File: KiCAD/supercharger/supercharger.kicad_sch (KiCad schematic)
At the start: 25 parts, among them J2 BAT, J4 UJC-H-G-SMT-1-P6-TR

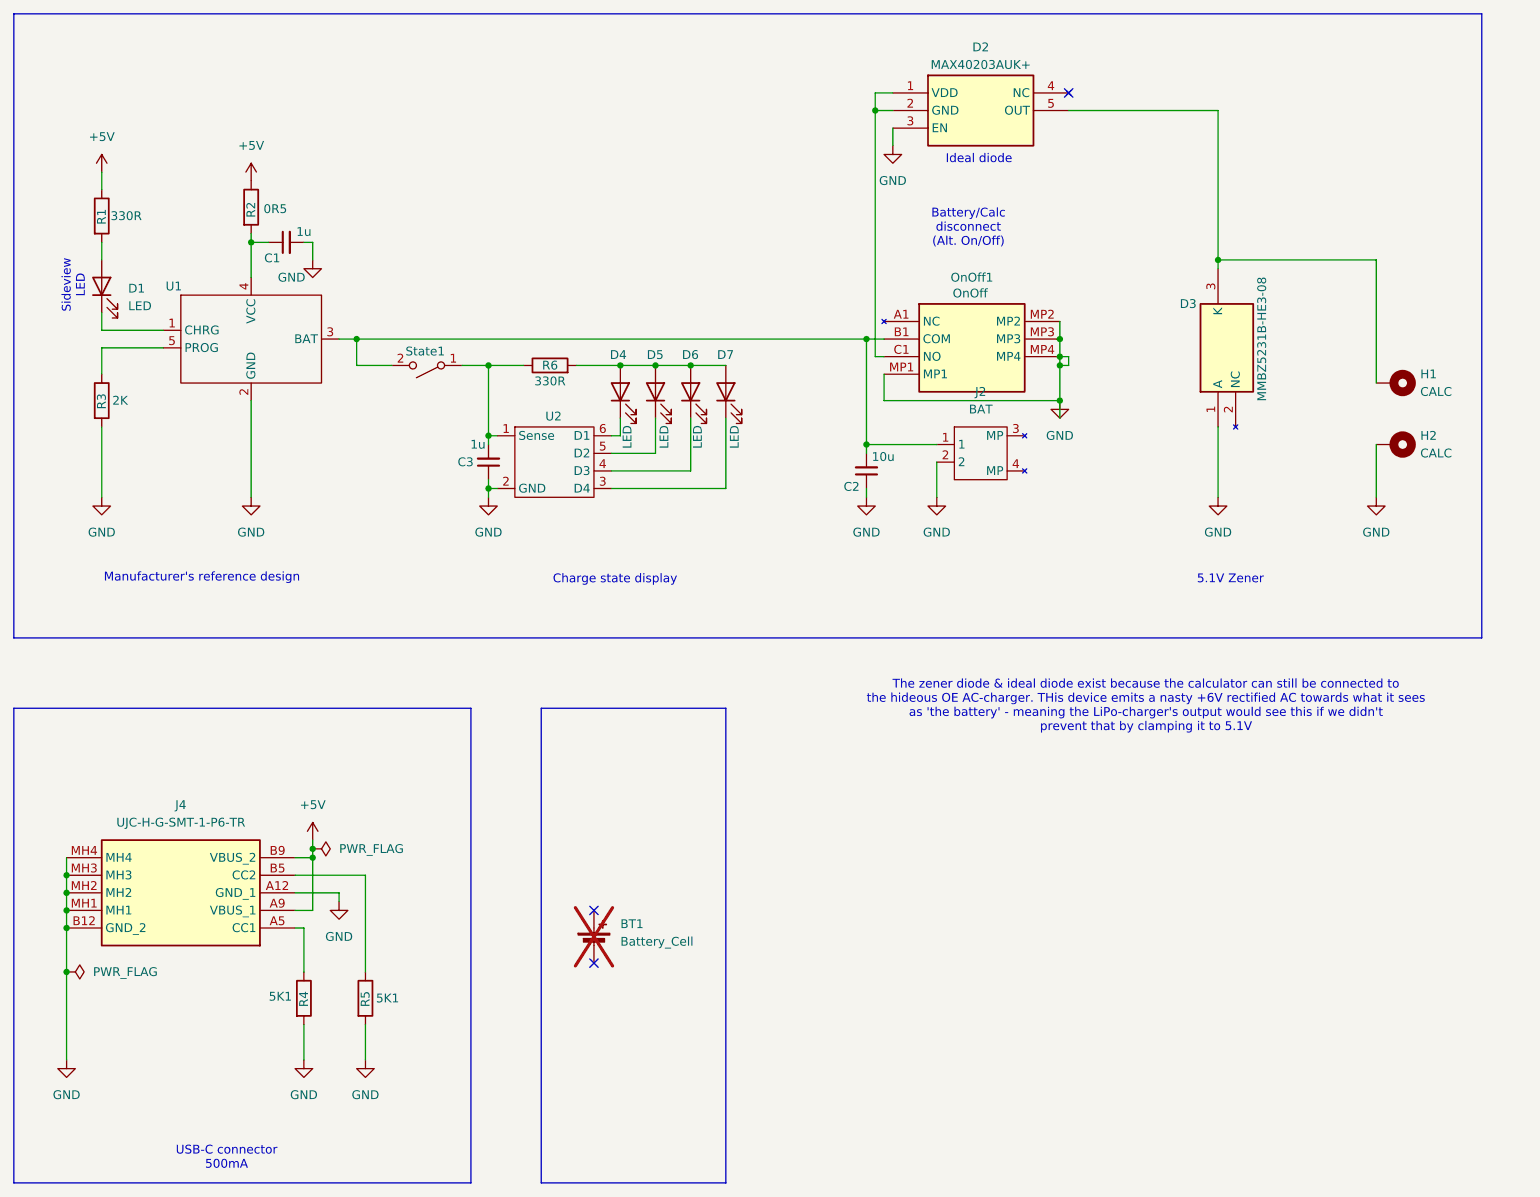
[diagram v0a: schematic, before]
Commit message: Schematic documentation update
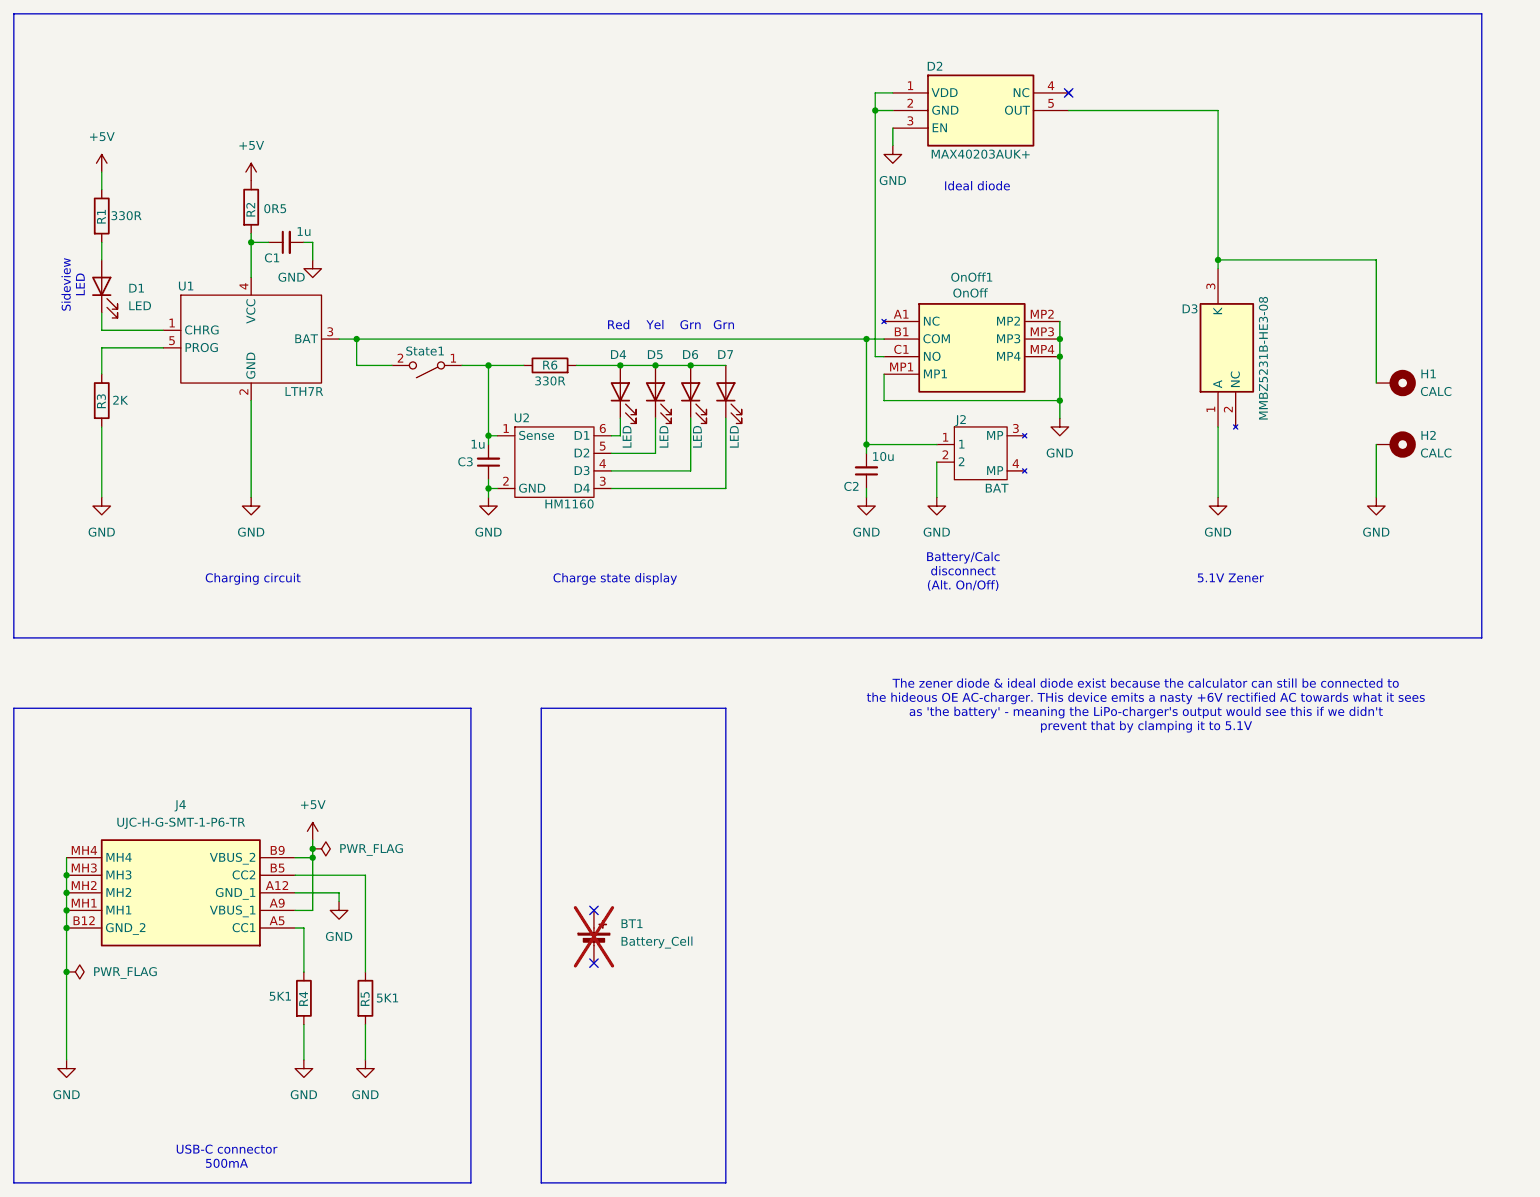
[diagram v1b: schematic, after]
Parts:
- U1: value ~ -> LTH7R
- U2: value ~ -> HM1160
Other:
- note added: "Charging circuit"
- note added: "Grn"
- note added: "Red"
- note added: "Yel"
- note removed: "Manufacturer's reference design"
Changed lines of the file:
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@@
 	)
 	(junction
-		(at 171.45 71.12)
-		(diameter 0)
-		(color 0 0 0 0)
-	)
-	(junction
 		(at 63.5 140.97)
 		(diameter 0)
@@
 	(wire
 		(pts
-			(xy 171.45 69.85) (xy 171.45 71.12)
+			(xy 171.45 69.85) (xy 171.45 76.2)
 		)
 		(stroke
@@
 	(wire
 		(pts
-			(xy 172.72 71.12) (xy 172.72 69.85)
-		)
-		(stroke
-			(width 0)
-			(type default)
-		)
-	)
-	(wire
-		(pts
 			(xy 67.31 147.32) (xy 60.96 147.32)
 		)
@@
 	(wire
 		(pts
-			(xy 171.45 71.12) (xy 171.45 76.2)
-		)
-		(stroke
-			(width 0)
-			(type default)
-		)
-	)
-	(wire
-		(pts
 			(xy 71.12 144.78) (xy 71.12 158.75)
 		)
@@
 	(wire
 		(pts
-			(xy 172.72 69.85) (xy 171.45 69.85)
-		)
-		(stroke
-			(width 0)
-			(type default)
-		)
-	)
-	(wire
-		(pts
 			(xy 146.05 76.2) (xy 171.45 76.2)
 		)
@@
 	(wire
 		(pts
-			(xy 171.45 78.74) (xy 171.45 76.2)
-		)
-		(stroke
-			(width 0)
-			(type default)
-		)
-	)
-	(wire
-		(pts
 			(xy 88.9 88.9) (xy 88.9 90.17)
 		)
@@
 	(wire
 		(pts
+			(xy 171.45 78.74) (xy 171.45 76.2)
+		)
+		(stroke
+			(width 0)
+			(type default)
+		)
+	)
+	(wire
+		(pts
 			(xy 153.67 85.09) (xy 153.67 90.17)
 		)
@@
 	(wire
 		(pts
-			(xy 172.72 71.12) (xy 171.45 71.12)
-		)
-		(stroke
-			(width 0)
-			(type default)
-		)
-	)
-	(wire
-		(pts
 			(xy 146.05 72.39) (xy 146.05 76.2)
 		)
@@
 		)
 	)
+	(text "Red"
+		(exclude_from_sim no)
+		(at 107.696 65.532 0)
+		(effects
+			(font
+				(size 1.27 1.27)
+			)
+		)
+	)
+	(text "Grn"
+		(exclude_from_sim no)
+		(at 118.11 65.532 0)
+		(effects
+			(font
+				(size 1.27 1.27)
+			)
+		)
+	)
 	(text "Sideview\nLED"
 		(exclude_from_sim no)
@@
 		)
 	)
+	(text "Grn"
+		(exclude_from_sim no)
+		(at 122.936 65.532 0)
+		(effects
+			(font
+				(size 1.27 1.27)
+			)
+		)
+	)
+	(text "Yel"
+		(exclude_from_sim no)
+		(at 113.03 65.532 0)
+		(effects
+			(font
+				(size 1.27 1.27)
+			)
+		)
+	)
 	(text "Battery/Calc\ndisconnect\n(Alt. On/Off)"
 		(exclude_from_sim no)
-		(at 158.242 51.308 0)
+		(at 157.48 101.092 0)
 		(effects
 			(font
@@
 	(text "Ideal diode"
 		(exclude_from_sim no)
-		(at 159.766 41.402 0)
+		(at 159.512 45.466 0)
 		(effects
 			(font
@@
 		)
 	)
-	(text "Manufacturer's reference design"
+	(text "Charging circuit"
 		(exclude_from_sim yes)
-		(at 47.498 101.854 0)
+		(at 54.864 102.108 0)
 		(effects
 			(font
@@
 		(dnp no)
 		(property "Reference" "D2"
-			(at 160.02 25.146 0)
+			(at 153.416 27.94 0)
 			(effects
 				(font
@@
 		)
 		(property "Value" "MAX40203AUK+"
-			(at 160.02 27.686 0)
+			(at 160.02 40.64 0)
 			(effects
 				(font
@@
 			)
 		)
-		(property "Datasheet" "~"
+		(property "Datasheet" "https://www.digikey.com/en/products/detail/omron-electronics-inc-emc-div/B3U-3000PM-B/2754806"
 			(at 80.01 71.12 0)
 			(effects
@@
 	(symbol
 		(lib_id "power:GND")
-		(at 171.45 76.2 0)
+		(at 171.45 78.74 0)
 		(unit 1)
 		(exclude_from_sim no)
@@
 		(fields_autoplaced yes)
 		(property "Reference" "#PWR014"
-			(at 171.45 82.55 0)
+			(at 171.45 85.09 0)
 			(effects
 				(font
@@
 		)
 		(property "Value" "GND"
-			(at 171.45 81.28 0)
+			(at 171.45 83.82 0)
 			(effects
 				(font
@@
 		)
 		(property "Footprint" ""
-			(at 171.45 76.2 0)
+			(at 171.45 78.74 0)
 			(effects
 				(font
@@
 		)
 		(property "Datasheet" ""
-			(at 171.45 76.2 0)
+			(at 171.45 78.74 0)
 			(effects
 				(font
@@
 		)
 		(property "Description" "Power symbol creates a global label with name \"GND\" , ground"
-			(at 171.45 76.2 0)
+			(at 171.45 78.74 0)
 			(effects
 				(font
@@
 		(on_board yes)
 		(dnp no)
-		(fields_autoplaced yes)
 		(property "Reference" "J2"
-			(at 160.02 74.93 0)
+			(at 157.226 78.994 0)
 			(effects
 				(font
@@
 		)
 		(property "Value" "BAT"
-			(at 160.02 77.47 0)
+			(at 162.306 88.9 0)
 			(effects
 				(font
@@
 		(dnp no)
 		(property "Reference" "D3"
-			(at 189.992 62.23 90)
+			(at 190.246 62.992 90)
 			(effects
 				(font
@@
 		)
 		(property "Value" "MMBZ5231B-HE3-08"
-			(at 200.66 67.31 0)
+			(at 200.914 70.104 0)
 			(effects
 				(font
@@
 			)
 		)
-		(property "Datasheet" "https://www.arrow.com/en/products/mmbz5231b-he3-08/vishay"
+		(property "Datasheet" "https://www.digikey.dk/da/products/detail/vishay-general-semiconductor-diodes-division/MMBZ5231B-HE3-08/4832016"
 			(at 389.23 60.96 0)
 			(effects
@@
 		(dnp no)
 		(property "Reference" "U1"
-			(at 43.434 59.69 0)
+			(at 45.212 59.69 0)
 			(effects
 				(font
@@
 			)
 		)
-		(property "Value" "~"
-			(at 67.31 64.1665 0)
+		(property "Value" "LTH7R"
+			(at 62.23 74.93 0)
 			(effects
 				(font
@@
 		(dnp no)
 		(property "Reference" "U2"
-			(at 98.298 78.486 0)
+			(at 93.726 78.74 0)
 			(effects
 				(font
@@
 			)
 		)
-		(property "Value" "~"
-			(at 98.425 78.74 0)
+		(property "Value" "HM1160"
+			(at 100.584 91.186 0)
 			(effects
 				(font
@@
 			)
 		)
-		(property "Datasheet" ""
+		(property "Datasheet" "https://www.alldatasheet.com/datasheet-pdf/view/1297703/HMSEMI/HM1160.html"
 			(at 96.52 78.74 0)
 			(effects

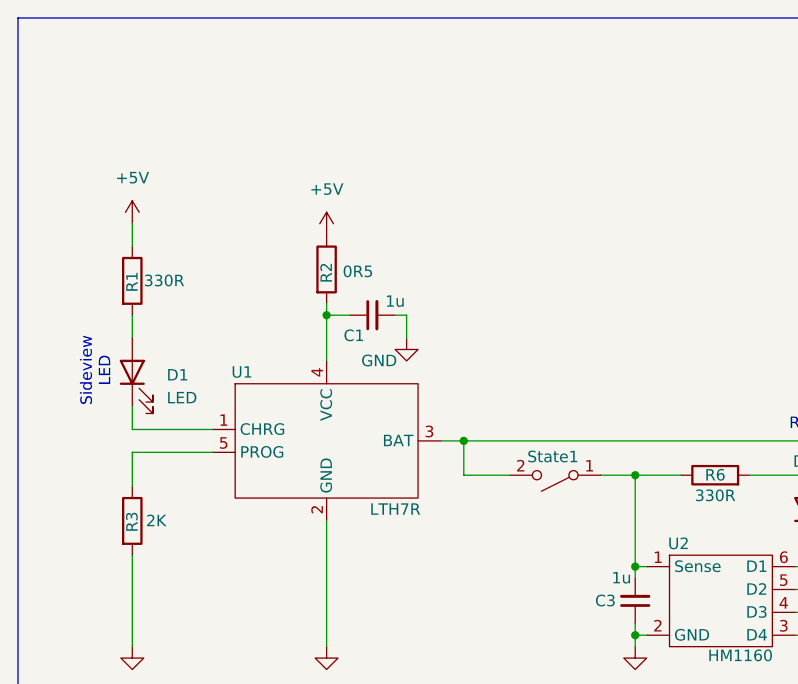
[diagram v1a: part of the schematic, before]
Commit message: Swapped LTH7R with STC4054 charger circuit
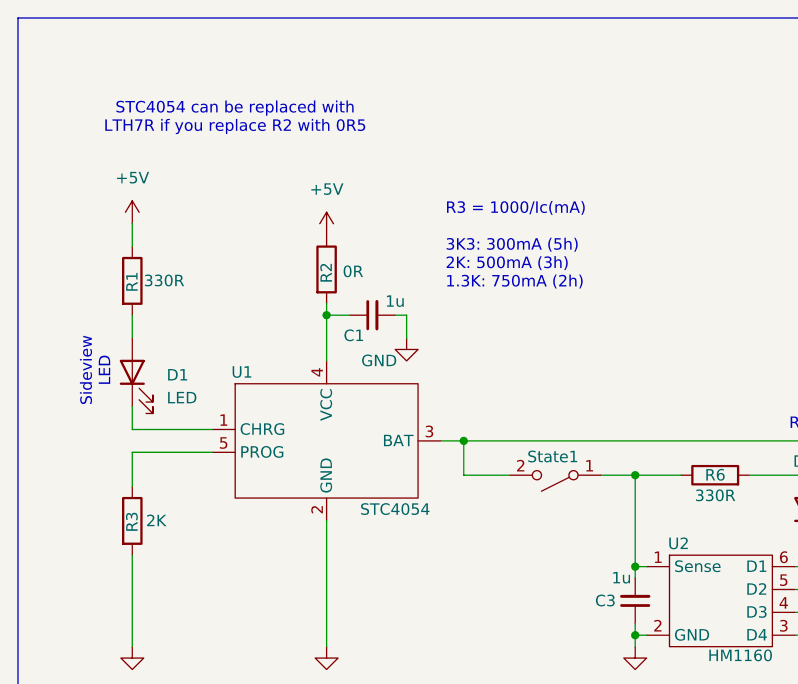
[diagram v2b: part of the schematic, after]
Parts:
- R2: value 0R5 -> 0R
- U1: value LTH7R -> STC4054
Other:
- note added: "R3 = 1000/Ic(mA) 3K3: 300mA (5h) 2K: 500mA (3h) 1.3K: 750mA (2h)"
- note added: "STC4054 can be replaced with LTH7R if you replace R2 with 0R5"
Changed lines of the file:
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@@
+		)
+	)
+	(text "R3 = 1000/Ic(mA)\n\n3K3: 300mA (5h)\n2K: 500mA (3h)\n1.3K: 750mA (2h)"
+		(exclude_from_sim no)
+		(at 67.818 45.72 0)
+		(effects
+			(font
+				(size 1.27 1.27)
+			)
+			(justify left)
 		)
 	)
@@
 		(exclude_from_sim no)
 		(at 159.512 45.466 0)
+		(effects
+			(font
+				(size 1.27 1.27)
+			)
+		)
+	)
+	(text "STC4054 can be replaced with \nLTH7R if you replace R2 with 0R5"
+		(exclude_from_sim no)
+		(at 44.45 31.496 0)
 		(effects
 			(font
@@
 			)
 		)
-		(property "Value" "LTH7R"
+		(property "Value" "STC4054"
 			(at 62.23 74.93 0)
 			(effects
@@
 			)
 		)
-		(property "Datasheet" "https://www.elcircuits.com/programmable-4v2-battery-charger-lth7r/"
+		(property "Datasheet" "file:///C:/Users/mfi/Downloads/stc4054-1.pdf"
 			(at 54.864 71.374 0)
 			(effects
@@
 			)
 		)
-		(property "Value" "0R5"
+		(property "Value" "0R"
 			(at 56.388 48.514 0)
 			(effects
